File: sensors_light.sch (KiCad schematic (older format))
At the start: 6 parts

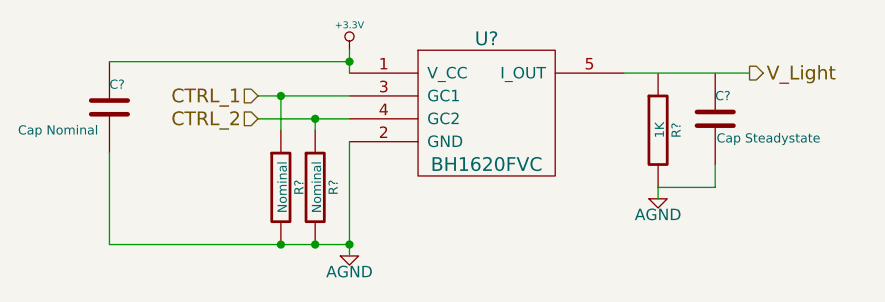
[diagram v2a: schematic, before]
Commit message: organized proc sheet I/O, organized I2C bus structure
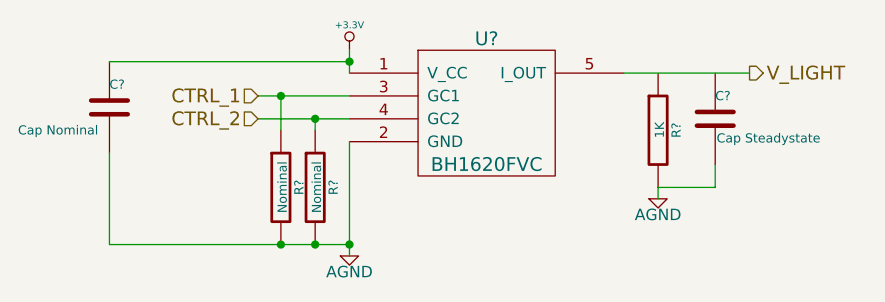
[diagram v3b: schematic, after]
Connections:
- net V_Light renamed V_LIGHT
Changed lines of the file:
@@
 $EndComp
 Text HLabel 4700 800  2    60   Output ~ 0
-V_Light
+V_LIGHT
 $Comp
 L AGND #PWR?
